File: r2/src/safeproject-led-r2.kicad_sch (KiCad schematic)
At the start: 14 parts, among them J1 2842142-4, J2 FH12-20S-0.5SH

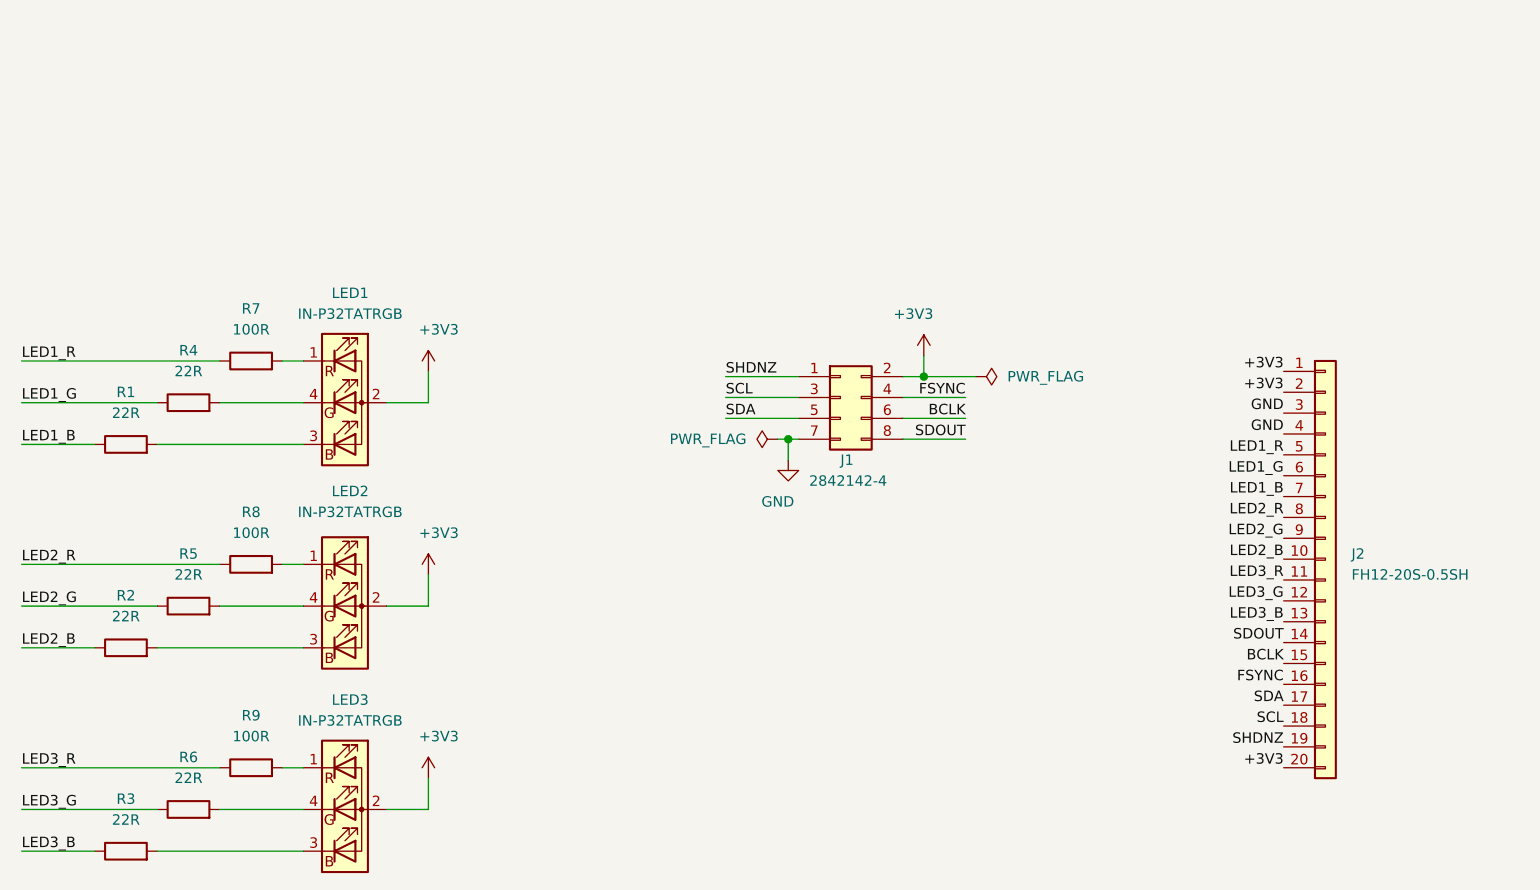
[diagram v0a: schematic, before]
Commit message: Rewire the board to use the new 5V line on FFC pin 20 for the LED power. Prevents us injecting LED switching noise into the 3V3 rail
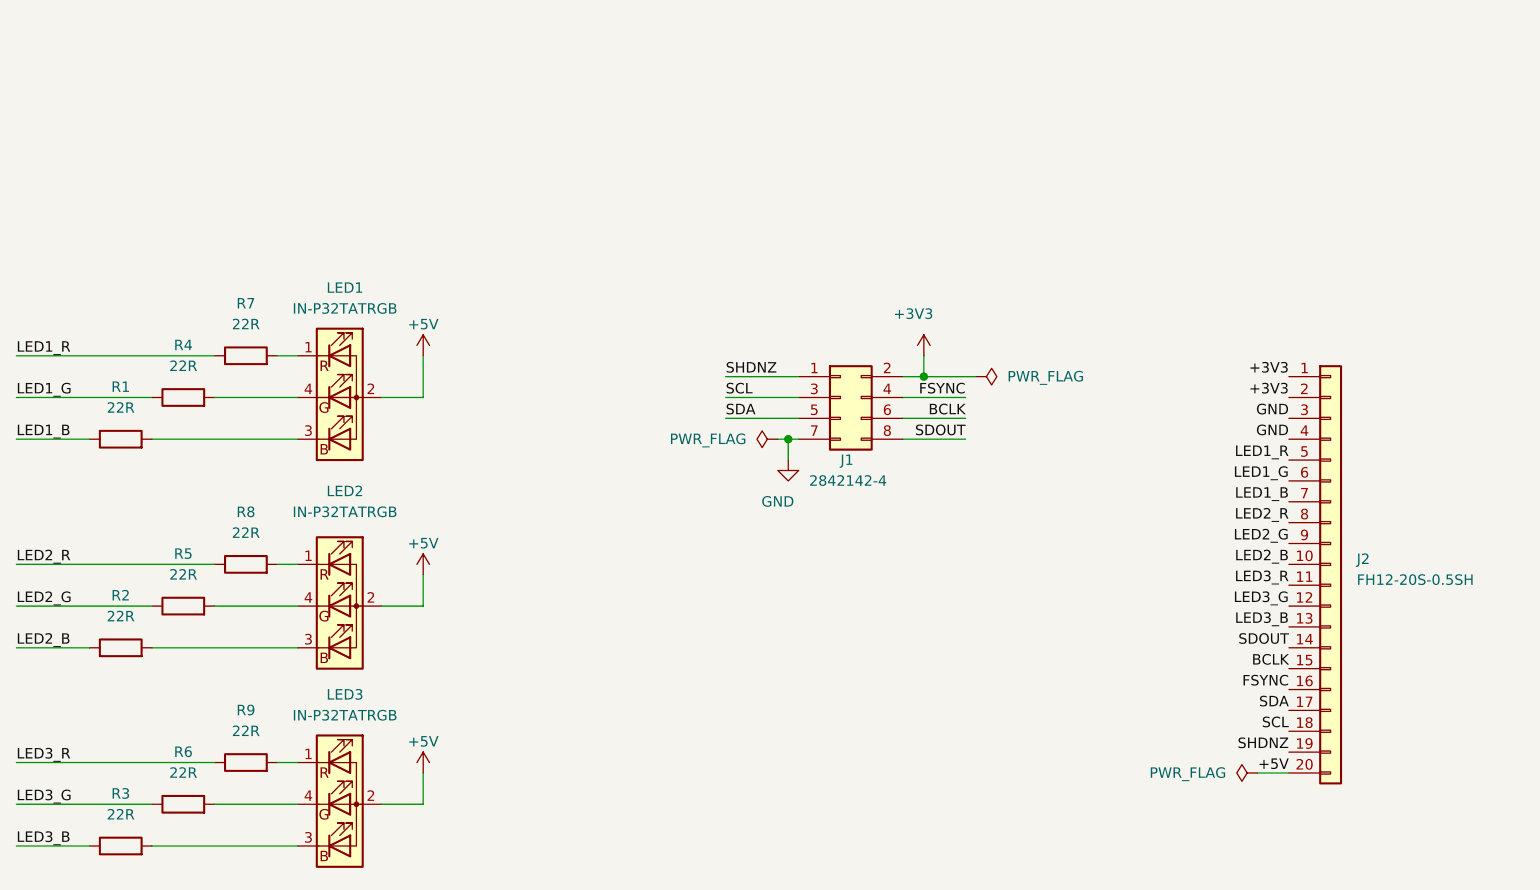
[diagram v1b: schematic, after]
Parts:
- R7, R8, R9: value 100R -> 22R
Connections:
- net +3V3: no longer J2.20 (Pin_20), LED1.2 (A), LED2.2 (A), LED3.2 (A)
- new net +5V: J2.20 (Pin_20), LED1.2 (A), LED2.2 (A), LED3.2 (A)
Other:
- moved on the sheet: J2, LED1, LED2, LED3, R1, R2, R3, R4, R5, R6, R7, R8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

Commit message: Add 200 to all designators to prevent collisoins in the panel
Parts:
- renumbered J1 to J201, J2 to J202, LED1 to LED201, LED2 to LED202, LED3 to LED203, R1 to R201, R2 to R202, R3 to R203, R4 to R204, R5 to R205, R6 to R206, R7 to R207, R8 to R208, R9 to R209
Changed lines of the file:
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@@
   (symbol (lib_id "Device:R") (at 87.63 80.01 90) (unit 1)
     (in_bom yes) (on_board yes)
-    (property "Reference" "R1" (id 0) (at 87.63 73.66 90))
+    (property "Reference" "R201" (id 0) (at 87.63 73.66 90))
     (property "Value" "22R" (id 1) (at 87.63 76.2 90))
     (property "Footprint" "Resistor_SMD:R_0603_1608Metric" (id 2) (at 87.63 81.788 90)
@@
   (symbol (lib_id "Device:R") (at 87.63 105.41 90) (unit 1)
     (in_bom yes) (on_board yes)
-    (property "Reference" "R2" (id 0) (at 87.63 99.06 90))
+    (property "Reference" "R202" (id 0) (at 87.63 99.06 90))
     (property "Value" "22R" (id 1) (at 87.63 101.6 90))
     (property "Footprint" "Resistor_SMD:R_0603_1608Metric" (id 2) (at 87.63 107.188 90)
@@
   (symbol (lib_id "Device:R") (at 87.63 129.54 90) (unit 1)
     (in_bom yes) (on_board yes)
-    (property "Reference" "R3" (id 0) (at 87.63 123.19 90))
+    (property "Reference" "R203" (id 0) (at 87.63 123.19 90))
     (property "Value" "22R" (id 1) (at 87.63 125.73 90))
     (property "Footprint" "Resistor_SMD:R_0603_1608Metric" (id 2) (at 87.63 131.318 90)
@@
   (symbol (lib_id "Device:R") (at 95.25 74.93 90) (unit 1)
     (in_bom yes) (on_board yes)
-    (property "Reference" "R4" (id 0) (at 95.25 68.58 90))
+    (property "Reference" "R204" (id 0) (at 95.25 68.58 90))
     (property "Value" "22R" (id 1) (at 95.25 71.12 90))
     (property "Footprint" "Resistor_SMD:R_0603_1608Metric" (id 2) (at 95.25 76.708 90)
@@
   (symbol (lib_id "Device:R") (at 95.25 100.33 90) (unit 1)
     (in_bom yes) (on_board yes)
-    (property "Reference" "R5" (id 0) (at 95.25 93.98 90))
+    (property "Reference" "R205" (id 0) (at 95.25 93.98 90))
     (property "Value" "22R" (id 1) (at 95.25 96.52 90))
     (property "Footprint" "Resistor_SMD:R_0603_1608Metric" (id 2) (at 95.25 102.108 90)
@@
   (symbol (lib_id "Device:R") (at 95.25 124.46 90) (unit 1)
     (in_bom yes) (on_board yes)
-    (property "Reference" "R6" (id 0) (at 95.25 118.11 90))
+    (property "Reference" "R206" (id 0) (at 95.25 118.11 90))
     (property "Value" "22R" (id 1) (at 95.25 120.65 90))
     (property "Footprint" "Resistor_SMD:R_0603_1608Metric" (id 2) (at 95.25 126.238 90)
@@
   (symbol (lib_id "Device:R") (at 102.87 69.85 90) (unit 1)
     (in_bom yes) (on_board yes)
-    (property "Reference" "R7" (id 0) (at 102.87 63.5 90))
+    (property "Reference" "R207" (id 0) (at 102.87 63.5 90))
     (property "Value" "22R" (id 1) (at 102.87 66.04 90))
     (property "Footprint" "Resistor_SMD:R_0603_1608Metric" (id 2) (at 102.87 71.628 90)
@@
   (symbol (lib_id "Device:R") (at 102.87 95.25 90) (unit 1)
     (in_bom yes) (on_board yes)
-    (property "Reference" "R8" (id 0) (at 102.87 88.9 90))
+    (property "Reference" "R208" (id 0) (at 102.87 88.9 90))
     (property "Value" "22R" (id 1) (at 102.87 91.44 90))
     (property "Footprint" "Resistor_SMD:R_0603_1608Metric" (id 2) (at 102.87 97.028 90)
@@
   (symbol (lib_id "Device:R") (at 102.87 119.38 90) (unit 1)
     (in_bom yes) (on_board yes)
-    (property "Reference" "R9" (id 0) (at 102.87 113.03 90))
+    (property "Reference" "R209" (id 0) (at 102.87 113.03 90))
     (property "Value" "22R" (id 1) (at 102.87 115.57 90))
     (property "Footprint" "Resistor_SMD:R_0603_1608Metric" (id 2) (at 102.87 121.158 90)
@@
   (symbol (lib_id "Connector_Generic:Conn_02x04_Odd_Even") (at 175.26 74.93 0) (unit 1)
     (in_bom yes) (on_board yes)
-    (property "Reference" "J1" (id 0) (at 175.26 82.55 0)
+    (property "Reference" "J201" (id 0) (at 175.26 82.55 0)
       (effects (font (size 1.27 1.27)) (justify left))
     )
@@
   (symbol (lib_id "Device:LED_RABG") (at 114.3 74.93 0) (unit 1)
     (in_bom yes) (on_board yes)
-    (property "Reference" "LED1" (id 0) (at 114.935 61.595 0))
+    (property "Reference" "LED201" (id 0) (at 114.935 61.595 0))
     (property "Value" "IN-P32TATRGB" (id 1) (at 114.935 64.135 0))
     (property "Footprint" "LED_SMD:LED_Avago_PLCC4_3.2x2.8mm_CW" (id 2) (at 114.3 76.2 0)
@@
   (symbol (lib_id "Device:LED_RABG") (at 114.3 100.33 0) (unit 1)
     (in_bom yes) (on_board yes)
-    (property "Reference" "LED2" (id 0) (at 114.935 86.36 0))
+    (property "Reference" "LED202" (id 0) (at 114.935 86.36 0))
     (property "Value" "IN-P32TATRGB" (id 1) (at 114.935 88.9 0))
     (property "Footprint" "LED_SMD:LED_Avago_PLCC4_3.2x2.8mm_CW" (id 2) (at 114.3 101.6 0)
@@
   (symbol (lib_id "Device:LED_RABG") (at 114.3 124.46 0) (unit 1)
     (in_bom yes) (on_board yes)
-    (property "Reference" "LED3" (id 0) (at 114.935 111.125 0))
+    (property "Reference" "LED203" (id 0) (at 114.935 111.125 0))
     (property "Value" "IN-P32TATRGB" (id 1) (at 114.935 113.665 0))
     (property "Footprint" "LED_SMD:LED_Avago_PLCC4_3.2x2.8mm_CW" (id 2) (at 114.3 125.73 0)
@@
   (symbol (lib_id "Connector_Generic:Conn_01x20") (at 234.95 95.25 0) (unit 1)
     (in_bom yes) (on_board yes)
-    (property "Reference" "J2" (id 0) (at 238.125 94.615 0)
+    (property "Reference" "J202" (id 0) (at 238.125 94.615 0)
       (effects (font (size 1.27 1.27)) (justify left))
     )
@@
     )
     (path "/e1a24511-a876-49f8-a44e-35e0f62d5b74"
-      (reference "J1") (unit 1) (value "2842142-4") (footprint "jeffmakes-footprints:PinSocket_2x04_P2.00mm_Vertical_SMD_Bottom_or_Top_Entry_AMPMODU")
+      (reference "J201") (unit 1) (value "2842142-4") (footprint "jeffmakes-footprints:PinSocket_2x04_P2.00mm_Vertical_SMD_Bottom_or_Top_Entry_AMPMODU")
     )
     (path "/dd841a3a-f14d-482c-bc64-6bfede2e6e4b"
-      (reference "J2") (unit 1) (value "FH12-20S-0.5SH") (footprint "Connector_FFC-FPC:Hirose_FH12-20S-0.5SH_1x20-1MP_P0.50mm_Horizontal")
+      (reference "J202") (unit 1) (value "FH12-20S-0.5SH") (footprint "Connector_FFC-FPC:Hirose_FH12-20S-0.5SH_1x20-1MP_P0.50mm_Horizontal")
     )
     (path "/f492d516-c771-407a-acac-9bdee10f94fd"
-      (reference "LED1") (unit 1) (value "IN-P32TATRGB") (footprint "LED_SMD:LED_Avago_PLCC4_3.2x2.8mm_CW")
+      (reference "LED201") (unit 1) (value "IN-P32TATRGB") (footprint "LED_SMD:LED_Avago_PLCC4_3.2x2.8mm_CW")
     )
     (path "/17e36525-3e8c-4238-86e4-81b4c2baf2bb"
-      (reference "LED2") (unit 1) (value "IN-P32TATRGB") (footprint "LED_SMD:LED_Avago_PLCC4_3.2x2.8mm_CW")
+      (reference "LED202") (unit 1) (value "IN-P32TATRGB") (footprint "LED_SMD:LED_Avago_PLCC4_3.2x2.8mm_CW")
     )
     (path "/0fac35d9-0dd4-4408-99a2-b56026e6c993"
-      (reference "LED3") (unit 1) (value "IN-P32TATRGB") (footprint "LED_SMD:LED_Avago_PLCC4_3.2x2.8mm_CW")
+      (reference "LED203") (unit 1) (value "IN-P32TATRGB") (footprint "LED_SMD:LED_Avago_PLCC4_3.2x2.8mm_CW")
     )
     (path "/cb9ccd1a-13ee-4624-9a4b-802e65d85af0"
-      (reference "R1") (unit 1) (value "22R") (footprint "Resistor_SMD:R_0603_1608Metric")
+      (reference "R201") (unit 1) (value "22R") (footprint "Resistor_SMD:R_0603_1608Metric")
     )
     (path "/58417487-3113-430b-9fc9-009d58e12415"
-      (reference "R2") (unit 1) (value "22R") (footprint "Resistor_SMD:R_0603_1608Metric")
+      (reference "R202") (unit 1) (value "22R") (footprint "Resistor_SMD:R_0603_1608Metric")
     )
     (path "/69397af2-1fee-4dec-9a03-ceb5f4e62e36"
-      (reference "R3") (unit 1) (value "22R") (footprint "Resistor_SMD:R_0603_1608Metric")
+      (reference "R203") (unit 1) (value "22R") (footprint "Resistor_SMD:R_0603_1608Metric")
     )
     (path "/c524c284-9623-4d8f-8e53-21acea5f02d2"
-      (reference "R4") (unit 1) (value "22R") (footprint "Resistor_SMD:R_0603_1608Metric")
+      (reference "R204") (unit 1) (value "22R") (footprint "Resistor_SMD:R_0603_1608Metric")
     )
     (path "/a7e2b58d-ba9e-4fb3-b19a-297697c34f7b"
-      (reference "R5") (unit 1) (value "22R") (footprint "Resistor_SMD:R_0603_1608Metric")
+      (reference "R205") (unit 1) (value "22R") (footprint "Resistor_SMD:R_0603_1608Metric")
     )
     (path "/c6476391-e7ce-4809-8a1f-47e170294b69"
-      (reference "R6") (unit 1) (value "22R") (footprint "Resistor_SMD:R_0603_1608Metric")
+      (reference "R206") (unit 1) (value "22R") (footprint "Resistor_SMD:R_0603_1608Metric")
     )
     (path "/37846301-7f60-44b4-9487-f411f7747188"
-      (reference "R7") (unit 1) (value "22R") (footprint "Resistor_SMD:R_0603_1608Metric")
+      (reference "R207") (unit 1) (value "22R") (footprint "Resistor_SMD:R_0603_1608Metric")
     )
     (path "/a87c8174-14da-4d1e-9d88-2fc40c19646c"
-      (reference "R8") (unit 1) (value "22R") (footprint "Resistor_SMD:R_0603_1608Metric")
+      (reference "R208") (unit 1) (value "22R") (footprint "Resistor_SMD:R_0603_1608Metric")
     )
     (path "/88245093-eea4-4fee-985c-b7064722ebde"
-      (reference "R9") (unit 1) (value "22R") (footprint "Resistor_SMD:R_0603_1608Metric")
-    )
-  )
+      (reference "R209") (unit 1) (value "22R") (footprint "Resistor_SMD:R_0603_1608Metric")
+    )
+  )

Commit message: Add mounting holes to schematic to get rid of any DRC bitching
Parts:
- added H201, H202, H203, H204: MountingHole_3.2mm_M3_DIN965, MountingHole:MountingHole_3.2mm_M3_DIN965, symbol Mechanical:MountingHole
- added H205, H206: MountingHole, symbol Mechanical:MountingHole
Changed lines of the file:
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@@
     (pin "1")
+  )
+  (symbol (lib_id "Mechanical:MountingHole") (at 114.3 30.48 0) (unit 1)
+    (in_bom yes) (on_board yes)
+    (property "Reference" "H201" (id 0) (at 118.11 29.8449 0)
+      (effects (font (size 1.27 1.27)) (justify left))
+    )
+    (property "Value" "MountingHole_3.2mm_M3_DIN965" (id 1) (at 118.11 32.3849 0)
+      (effects (font (size 1.27 1.27)) (justify left))
+    )
+    (property "Footprint" "MountingHole:MountingHole_3.2mm_M3_DIN965" (id 2) (at 114.3 30.48 0)
+      (effects (font (size 1.27 1.27)) hide)
+    )
+    (property "Datasheet" "~" (id 3) (at 114.3 30.48 0)
+      (effects (font (size 1.27 1.27)) hide)
+    )
+  )
+  (symbol (lib_id "Mechanical:MountingHole") (at 114.3 36.83 0) (unit 1)
+    (in_bom yes) (on_board yes)
+    (property "Reference" "H202" (id 0) (at 118.11 36.1949 0)
+      (effects (font (size 1.27 1.27)) (justify left))
+    )
+    (property "Value" "MountingHole_3.2mm_M3_DIN965" (id 1) (at 118.11 38.7349 0)
+      (effects (font (size 1.27 1.27)) (justify left))
+    )
+    (property "Footprint" "MountingHole:MountingHole_3.2mm_M3_DIN965" (id 2) (at 114.3 36.83 0)
+      (effects (font (size 1.27 1.27)) hide)
+    )
+    (property "Datasheet" "~" (id 3) (at 114.3 36.83 0)
+      (effects (font (size 1.27 1.27)) hide)
+    )
+  )
+  (symbol (lib_id "Mechanical:MountingHole") (at 114.3 43.18 0) (unit 1)
+    (in_bom yes) (on_board yes)
+    (property "Reference" "H203" (id 0) (at 118.11 42.5449 0)
+      (effects (font (size 1.27 1.27)) (justify left))
+    )
+    (property "Value" "MountingHole_3.2mm_M3_DIN965" (id 1) (at 118.11 45.0849 0)
+      (effects (font (size 1.27 1.27)) (justify left))
+    )
+    (property "Footprint" "MountingHole:MountingHole_3.2mm_M3_DIN965" (id 2) (at 114.3 43.18 0)
+      (effects (font (size 1.27 1.27)) hide)
+    )
+    (property "Datasheet" "~" (id 3) (at 114.3 43.18 0)
+      (effects (font (size 1.27 1.27)) hide)
+    )
+  )
+  (symbol (lib_id "Mechanical:MountingHole") (at 114.3 49.53 0) (unit 1)
+    (in_bom yes) (on_board yes)
+    (property "Reference" "H204" (id 0) (at 118.11 48.8949 0)
+      (effects (font (size 1.27 1.27)) (justify left))
+    )
+    (property "Value" "MountingHole_3.2mm_M3_DIN965" (id 1) (at 118.11 51.4349 0)
+      (effects (font (size 1.27 1.27)) (justify left))
+    )
+    (property "Footprint" "MountingHole:MountingHole_3.2mm_M3_DIN965" (id 2) (at 114.3 49.53 0)
+      (effects (font (size 1.27 1.27)) hide)
+    )
+    (property "Datasheet" "~" (id 3) (at 114.3 49.53 0)
+      (effects (font (size 1.27 1.27)) hide)
+    )
+  )
+  (symbol (lib_id "Mechanical:MountingHole") (at 165.1 30.48 0) (unit 1)
+    (in_bom yes) (on_board yes)
+    (property "Reference" "H205" (id 0) (at 168.91 29.8449 0)
+      (effects (font (size 1.27 1.27)) (justify left))
+    )
+    (property "Value" "MountingHole" (id 1) (at 168.91 32.3849 0)
+      (effects (font (size 1.27 1.27)) (justify left))
+    )
+    (property "Footprint" "" (id 2) (at 165.1 30.48 0)
+      (effects (font (size 1.27 1.27)) hide)
+    )
+    (property "Datasheet" "~" (id 3) (at 165.1 30.48 0)
+      (effects (font (size 1.27 1.27)) hide)
+    )
+  )
+  (symbol (lib_id "Mechanical:MountingHole") (at 165.1 36.83 0) (unit 1)
+    (in_bom yes) (on_board yes)
+    (property "Reference" "H206" (id 0) (at 168.91 36.1949 0)
+      (effects (font (size 1.27 1.27)) (justify left))
+    )
+    (property "Value" "MountingHole" (id 1) (at 168.91 38.7349 0)
+      (effects (font (size 1.27 1.27)) (justify left))
+    )
+    (property "Footprint" "" (id 2) (at 165.1 36.83 0)
+      (effects (font (size 1.27 1.27)) hide)
+    )
+    (property "Datasheet" "~" (id 3) (at 165.1 36.83 0)
+      (effects (font (size 1.27 1.27)) hide)
+    )
   )
   (symbol (lib_id "Device:R") (at 87.63 80.01 90) (unit 1)
@@
       (reference "#PWR0105") (unit 1) (value "+3V3") (footprint "")
     )
+    (path "/214c1eae-cb75-4585-a61c-bbaa84266b34"
+      (reference "H201") (unit 1) (value "MountingHole_3.2mm_M3_DIN965") (footprint "MountingHole:MountingHole_3.2mm_M3_DIN965")
+    )
+    (path "/29b07526-3b8f-46ab-9118-ddd441d2f843"
+      (reference "H202") (unit 1) (value "MountingHole_3.2mm_M3_DIN965") (footprint "MountingHole:MountingHole_3.2mm_M3_DIN965")
+    )
+    (path "/9875f2ff-0604-4fbb-8b78-88ef54902074"
+      (reference "H203") (unit 1) (value "MountingHole_3.2mm_M3_DIN965") (footprint "MountingHole:MountingHole_3.2mm_M3_DIN965")
+    )
+    (path "/36b4f85a-1ddd-4fa4-9947-9fe4637a0969"
+      (reference "H204") (unit 1) (value "MountingHole_3.2mm_M3_DIN965") (footprint "MountingHole:MountingHole_3.2mm_M3_DIN965")
+    )
+    (path "/b58a2690-8660-4d8f-8af0-069247d4b235"
+      (reference "H205") (unit 1) (value "MountingHole") (footprint "")
+    )
+    (path "/1cc1bbdb-c0ab-4784-9028-d04976651e40"
+      (reference "H206") (unit 1) (value "MountingHole") (footprint "")
+    )
     (path "/e1a24511-a876-49f8-a44e-35e0f62d5b74"

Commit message: Correct value for board-to-board connector
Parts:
- J201: value 2842142-4 -> 2314844-8
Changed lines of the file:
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@@
       (effects (font (size 1.27 1.27)) (justify left))
     )
-    (property "Value" "2842142-4" (id 1) (at 171.45 85.09 0)
+    (property "Value" "2314844-8" (id 1) (at 171.45 85.09 0)
       (effects (font (size 1.27 1.27)) (justify left))
     )
@@
     )
     (path "/e1a24511-a876-49f8-a44e-35e0f62d5b74"
-      (reference "J201") (unit 1) (value "2842142-4") (footprint "jeffmakes-footprints:PinSocket_2x04_P2.00mm_Vertical_SMD_Bottom_or_Top_Entry_AMPMODU")
+      (reference "J201") (unit 1) (value "2314844-8") (footprint "jeffmakes-footprints:PinSocket_2x04_P2.00mm_Vertical_SMD_Bottom_or_Top_Entry_AMPMODU")
     )
     (path "/dd841a3a-f14d-482c-bc64-6bfede2e6e4b"

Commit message: Correct name for FFC connector
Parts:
- J202: value FH12-20S-0.5SH -> FH12A-20S-0.5SH
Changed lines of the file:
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@@
       (effects (font (size 1.27 1.27)) (justify left))
     )
-    (property "Value" "FH12-20S-0.5SH" (id 1) (at 238.125 97.155 0)
+    (property "Value" "FH12A-20S-0.5SH" (id 1) (at 238.125 97.155 0)
       (effects (font (size 1.27 1.27)) (justify left))
     )
@@
     )
     (path "/dd841a3a-f14d-482c-bc64-6bfede2e6e4b"
-      (reference "J202") (unit 1) (value "FH12-20S-0.5SH") (footprint "Connector_FFC-FPC:Hirose_FH12-20S-0.5SH_1x20-1MP_P0.50mm_Horizontal")
+      (reference "J202") (unit 1) (value "FH12A-20S-0.5SH") (footprint "Connector_FFC-FPC:Hirose_FH12-20S-0.5SH_1x20-1MP_P0.50mm_Horizontal")
     )
     (path "/f492d516-c771-407a-acac-9bdee10f94fd"
